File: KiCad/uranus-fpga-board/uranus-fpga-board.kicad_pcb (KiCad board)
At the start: 2 copper layers, 1 part

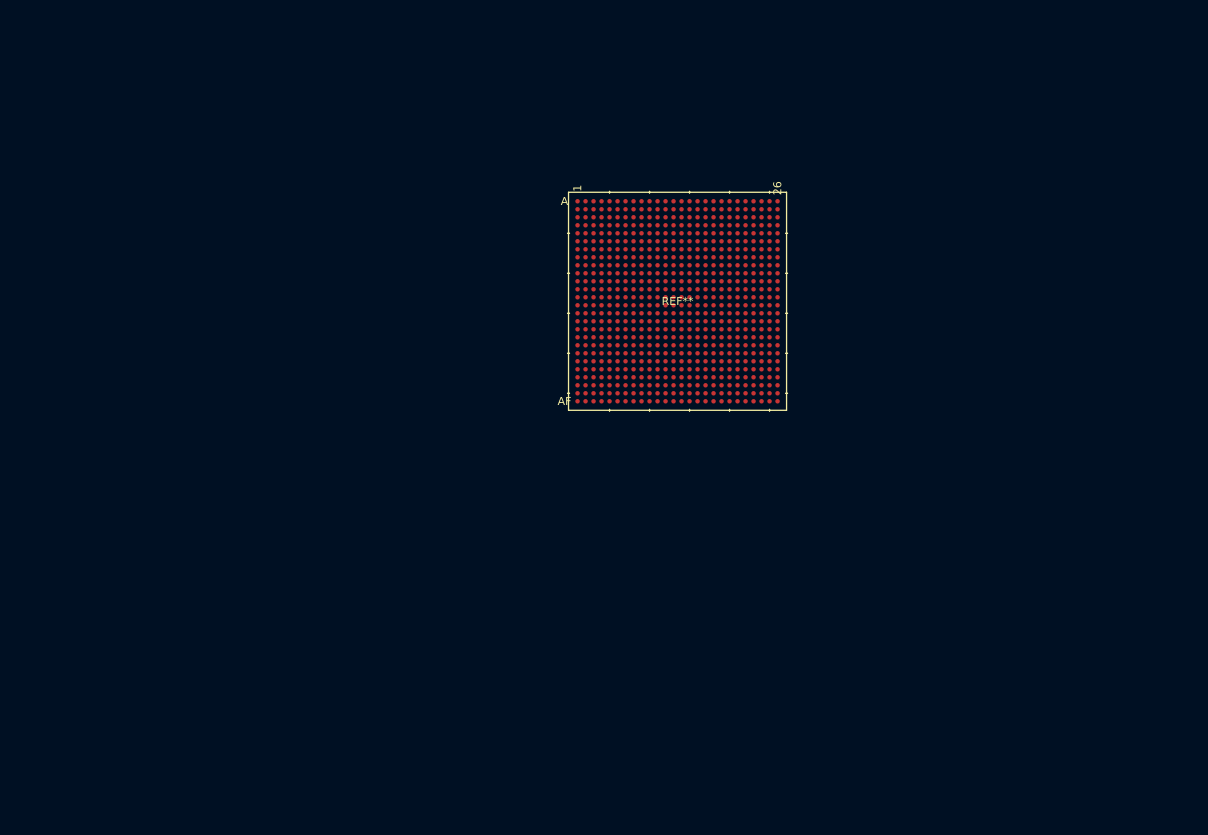
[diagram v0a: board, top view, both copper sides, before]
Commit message: updated journal entries and BOM
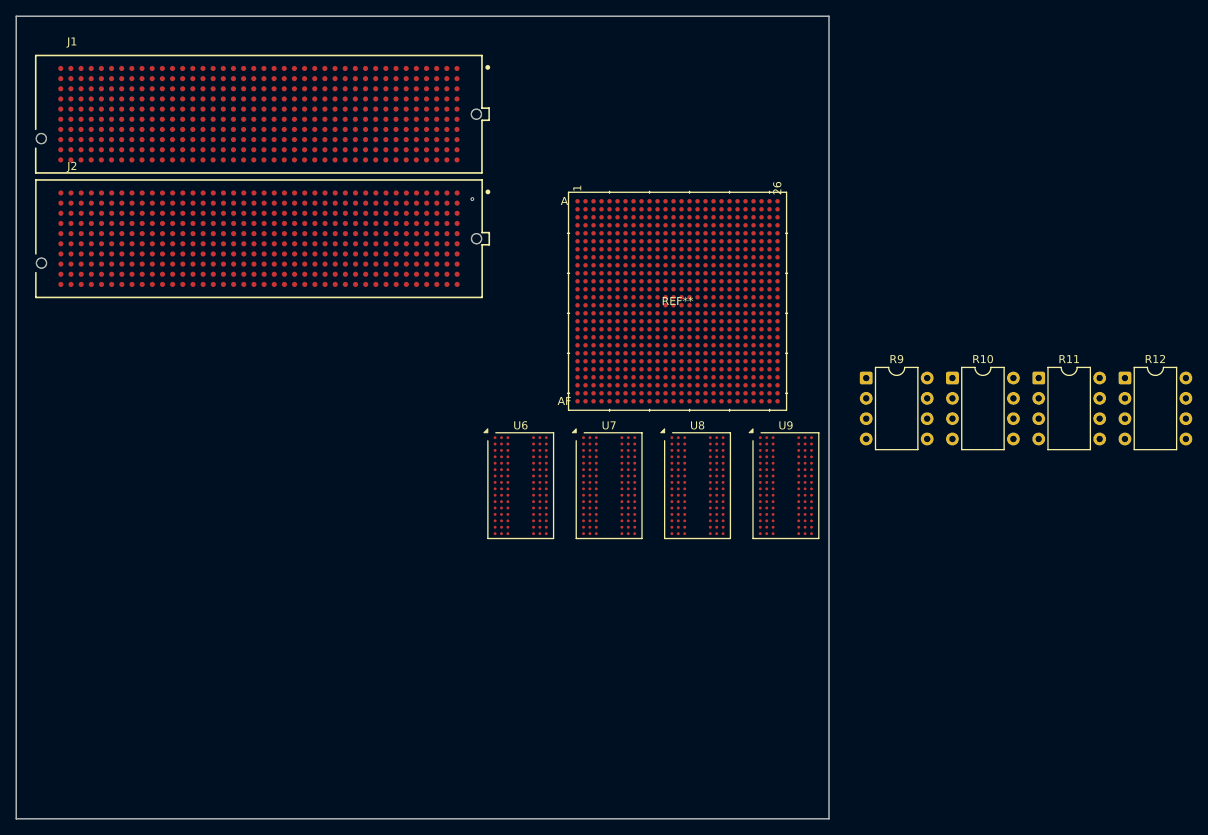
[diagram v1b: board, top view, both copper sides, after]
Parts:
- added J1: ASP-134488-01, FMC-HPC:SAMTEC_ASP-134488-01, F.Cu at (83.2, 75.1)
- added J2: ASP-134488-01, FMC-HPC:SAMTEC_ASP-134488-01, F.Cu at (83.2, 90.7)
- added R10: 240Ω, Package_DIP:DIP-8_W7.62mm, F.Cu at (169.9, 108.1)
- added R11: 240Ω, Package_DIP:DIP-8_W7.62mm, F.Cu at (180.6, 108.1)
- added R12: 240Ω, Package_DIP:DIP-8_W7.62mm, F.Cu at (191.4, 108.1)
- added R9: 240Ω, Package_DIP:DIP-8_W7.62mm, F.Cu at (159.1, 108.1)
- added U6: AS4C256M16D3, Package_BGA:FBGA-96_8x13mm_Layout9x16_P0.8mm, F.Cu at (115.9, 121.5)
- added U7: AS4C256M16D3, Package_BGA:FBGA-96_8x13mm_Layout9x16_P0.8mm, F.Cu at (126.9, 121.5)
- added U8: AS4C256M16D3, Package_BGA:FBGA-96_8x13mm_Layout9x16_P0.8mm, F.Cu at (138.0, 121.5)
- added U9: AS4C256M16D3, Package_BGA:FBGA-96_8x13mm_Layout9x16_P0.8mm, F.Cu at (149.0, 121.5)
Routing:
- net (no net): vias 0 -> 1
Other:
- board outline added: 101.6 x 100.3 mm
- copper layers 2 -> 8
